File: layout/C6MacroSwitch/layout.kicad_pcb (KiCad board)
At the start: 2 copper layers, 70 x 85 mm, 32 parts, among them J1 S2B-PH-K-S(LF)(SN), J2 61300211121, SW1 CPG135001D01, SW2 CPG135001D01, SW3 CPG135001D01, SW4 CPG135001D01, SW5 CPG135001D01, SW6 CPG135001D01, SW7 TSA061B2808B, SW8 TSA061B2808B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

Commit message: feat(zener): resync layout KiCad ai LED 0603
Rigenerato il .kicad_pcb dopo il cambio package dei LED: i footprint
D_CHG/D_LED passano da LED_0402_1005Metric a LED_0603_1608Metric,
piazzamento preservato. Allinea il layout al design.
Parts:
- D1: value VLMS1500-GS08 -> LED RED; footprint kicad_libraries_kicad-footprints_LED_SMD@9.0.3:LED_0402_1005Metric -> kicad_libraries_kicad-footprints_LED_SMD@9.0.3:LED_0603_1608Metric
- D2: value VLMG1500-GS08 -> LED GREEN; footprint kicad_libraries_kicad-footprints_LED_SMD@9.0.3:LED_0402_1005Metric -> kicad_libraries_kicad-footprints_LED_SMD@9.0.3:LED_0603_1608Metric

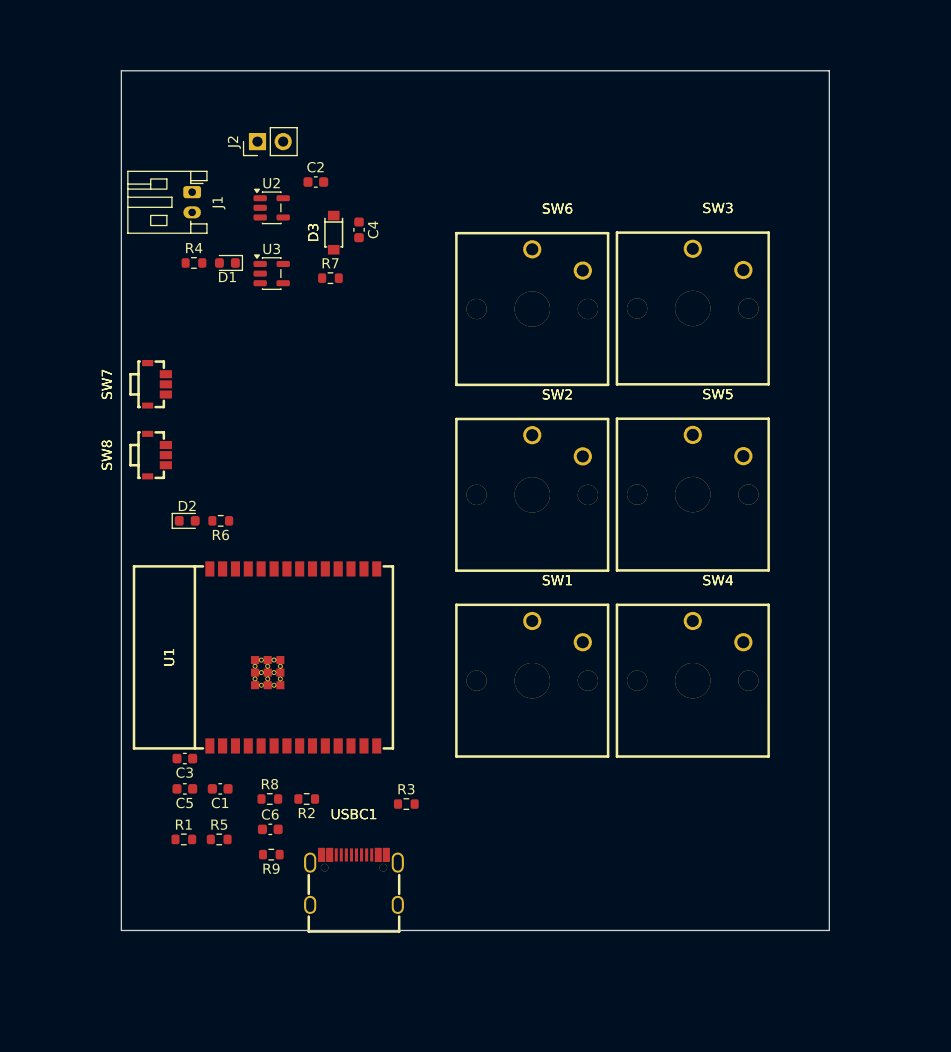
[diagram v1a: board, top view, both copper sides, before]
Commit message: feat(zener): piazza i 6 Choc su griglia 1u 2x3 (pitch 19.05mm)
Switch macro disposti su griglia 2x3 a pitch MX 1u (19.05mm) con stessa
rotazione; origine footprint compensata per l'offset del polo centrale
(-2.5,+4.85) così i centri keycap cadono su coordinate pulite. Nessuna
collisione Choc-Choc.

WIP floorplan: il cluster si sovrappone al supporto (ESP32/passivi),
da riposizionare sotto i tasti nella fase di layout finale.
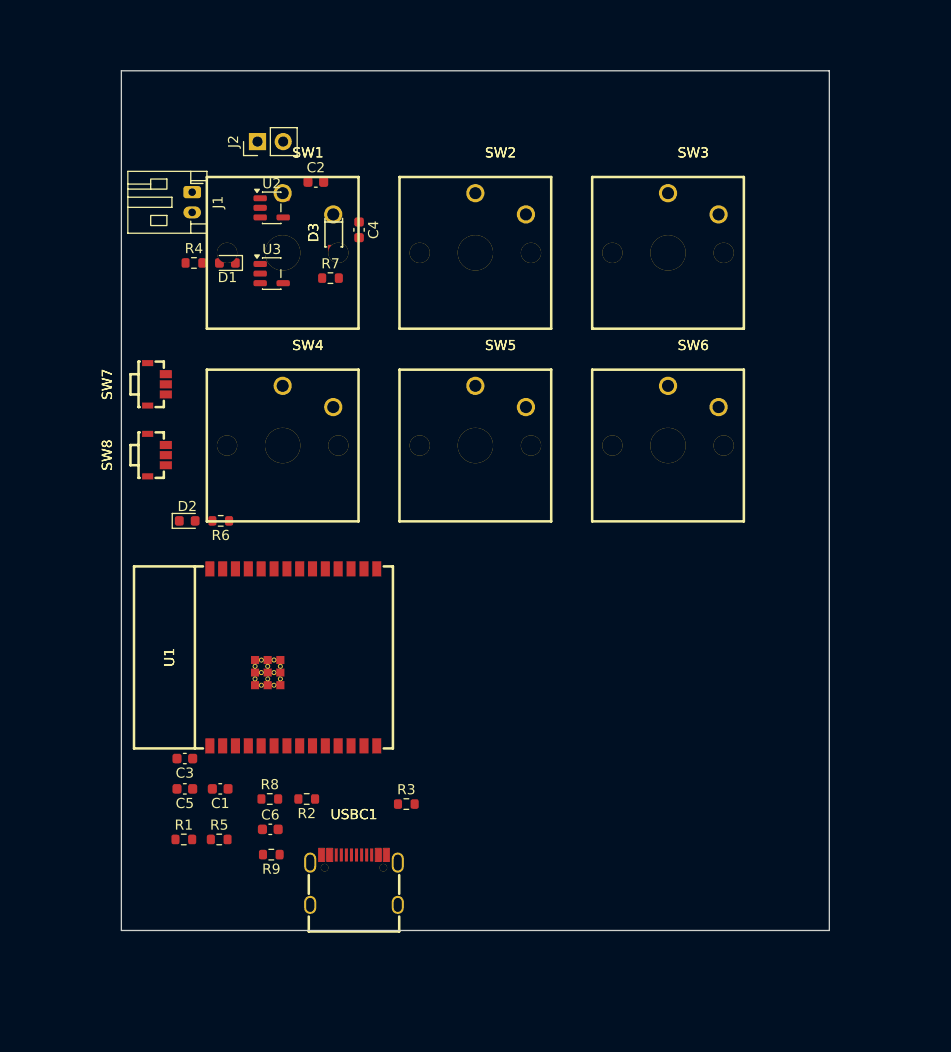
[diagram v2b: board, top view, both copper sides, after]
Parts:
- moved SW1 49.0 mm to (143.4, 63.1)
- moved SW4 46.7 mm to (143.4, 82.2)
- moved SW2 24.6 mm to (162.5, 63.1)
- moved SW5 22.0 mm to (162.5, 82.2)
- moved SW6 19.0 mm to (181.6, 82.2)
- moved SW3 6.02 mm to (181.6, 63.1)
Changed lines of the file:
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@@
 	(footprint "iu3qez_esp32c6_components_KailhChoc:KEY-TH_CPG135001D0X"
 		(layer "F.Cu")
-		(at 168.125 105.45)
+		(at 143.45 63.15)
 		(property "Reference" "SW1"
 			(at 0 -5.05 0)
@@
 	(footprint "iu3qez_esp32c6_components_KailhChoc:KEY-TH_CPG135001D0X"
 		(layer "F.Cu")
-		(at 184 68.65)
+		(at 181.55 63.15)
 		(property "Reference" "SW3"
 			(at 0 -5.05 0)
@@
 	(footprint "iu3qez_esp32c6_components_KailhChoc:KEY-TH_CPG135001D0X"
 		(layer "F.Cu")
-		(at 168.125 87.07675)
+		(at 162.5 63.15)
 		(property "Reference" "SW2"
 			(at 0 -5.05 0)
@@
 	(footprint "iu3qez_esp32c6_components_KailhChoc:KEY-TH_CPG135001D0X"
 		(layer "F.Cu")
-		(at 184 105.45)
+		(at 143.45 82.2)
 		(property "Reference" "SW4"
 			(at 0 -5.05 0)
@@
 	(footprint "iu3qez_esp32c6_components_KailhChoc:KEY-TH_CPG135001D0X"
 		(layer "F.Cu")
-		(at 184 87.05)
+		(at 162.5 82.2)
 		(property "Reference" "SW5"
 			(at 0 -5.05 0)
@@
 	(footprint "iu3qez_esp32c6_components_KailhChoc:KEY-TH_CPG135001D0X"
 		(layer "F.Cu")
-		(at 168.125 68.7035)
+		(at 181.55 82.2)
 		(property "Reference" "SW6"
 			(at 0 -5.05 0)

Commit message: feat(zener): primo sbroglio e layout della board
Prima passata di routing manuale in KiCad: 151 tracce, 17 via e 3 zone
di rame, con relative net class e impostazioni di progetto.
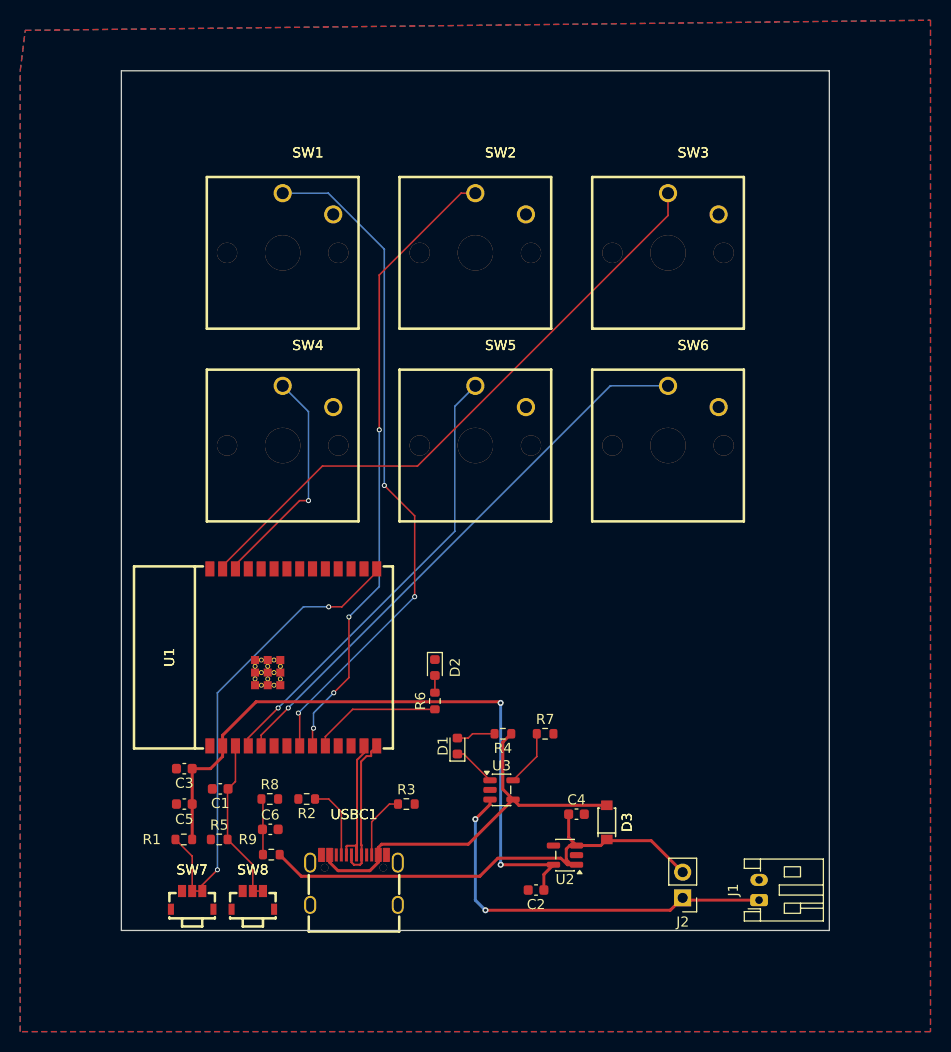
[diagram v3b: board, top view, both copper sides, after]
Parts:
- moved J1 89.7 mm to (188.1, 132.0), turned to 90 degrees
- moved J2 85.8 mm to (180.5, 131.8), turned to 180 degrees
- moved C2 73.3 mm to (166.0, 131.0), turned to 180 degrees
- moved U2 70.3 mm to (168.9, 127.5), turned to 180 degrees
- moved D3 64.3 mm to (173.0, 124.3), turned to 90 degrees
- moved C4 61.6 mm to (170.0, 123.5), turned to 0 degrees
- moved U3 55.9 mm to (162.6, 121.1)
- moved R4 55.7 mm to (162.7, 115.5), turned to 180 degrees
- moved D1 52.9 mm to (158.2, 116.8), turned to 90 degrees
- moved SW7 51.1 mm to (132.0, 132.0), turned to 180 degrees
- moved R7 49.8 mm to (166.9, 115.5)
- moved SW8 45.0 mm to (138.0, 132.0), turned to 180 degrees
- moved D2 28.5 mm to (156.0, 109.0), turned to -90 degrees
- moved R6 27.7 mm to (156.0, 112.3), turned to 90 degrees
- moved C5 1.50 mm to (131.2, 122.5)
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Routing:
- net KEY1: track 0.00 -> 67.5 mm, vias 0 -> 3
- net 3V3: track 0.00 -> 65.9 mm, vias 0 -> 2
- net KEY2: track 0.00 -> 62.1 mm, vias 0 -> 4
- net KEY3: track 0.00 -> 60.9 mm
- net KEY6: track 0.00 -> 55.6 mm, vias 0 -> 1
- net VBAT_SW: track 0.00 -> 50.1 mm
- net BOOT: track 0.00 -> 48.1 mm, vias 0 -> 2
- net KEY5: track 0.00 -> 44.9 mm, vias 0 -> 1
- net VBUS: track 0.00 -> 39.8 mm
- net VBAT: track 0.00 -> 39.6 mm, vias 0 -> 2
- net KEY4: track 0.00 -> 22.7 mm, vias 0 -> 1
- net EN: track 0.00 -> 16.7 mm
- net USB_D_P: track 0.00 -> 14.4 mm
- net USB_D_N: track 0.00 -> 13.8 mm
- net LED: track 0.00 -> 12.9 mm
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- added copper zone on B.Cu, net GND
- added copper zone on F.Cu, net GND

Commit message: fix(zener): review fixes — LDO caps 10uF, reverse-battery Q/D options, IO8 strap pullup, LED to IO10, Choc NPTH+courtyard
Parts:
- added D3: 1N5817W, iu3qez_esp32c6_components_SS1N5817W:SOD-123_L2.7-W1.6-LS3.6-RD, F.Cu at (197.2, 134.3)
- added Q1: AO3401A, iu3qez_esp32c6_components_AO3401A:SOT-23, F.Cu at (197.0, 127.7)
- added R6: ERJ-3EKF1002V, kicad_libraries_kicad-footprints_Resistor_SMD@9.0.3:R_0603_1608Metric, F.Cu at (200.9, 134.5)
- C4, C5: value GCM188R71E105KA64D -> GRM188Z71A106KA73D
- renumbered D3 to D4, R9 to R10, R6 to R7, R7 to R8, R8 to R9
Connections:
- J1 pad 1: VBAT -> BAT_RAW
- U1 pad 10: LED -> IO8_STRAP
- U1 pad 11: U1.IO10 -> LED

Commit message: fix(zener): LDO caps to 0805 for DC-bias derating margin
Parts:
- C4, C5: value GRM188Z71A106KA73D -> GRM21BZ71E106KE15K; footprint kicad_libraries_kicad-footprints_Capacitor_SMD@9.0.3:C_0603_1608Metric -> kicad_libraries_kicad-footprints_Capacitor_SMD@9.0.3:C_0805_2012Metric

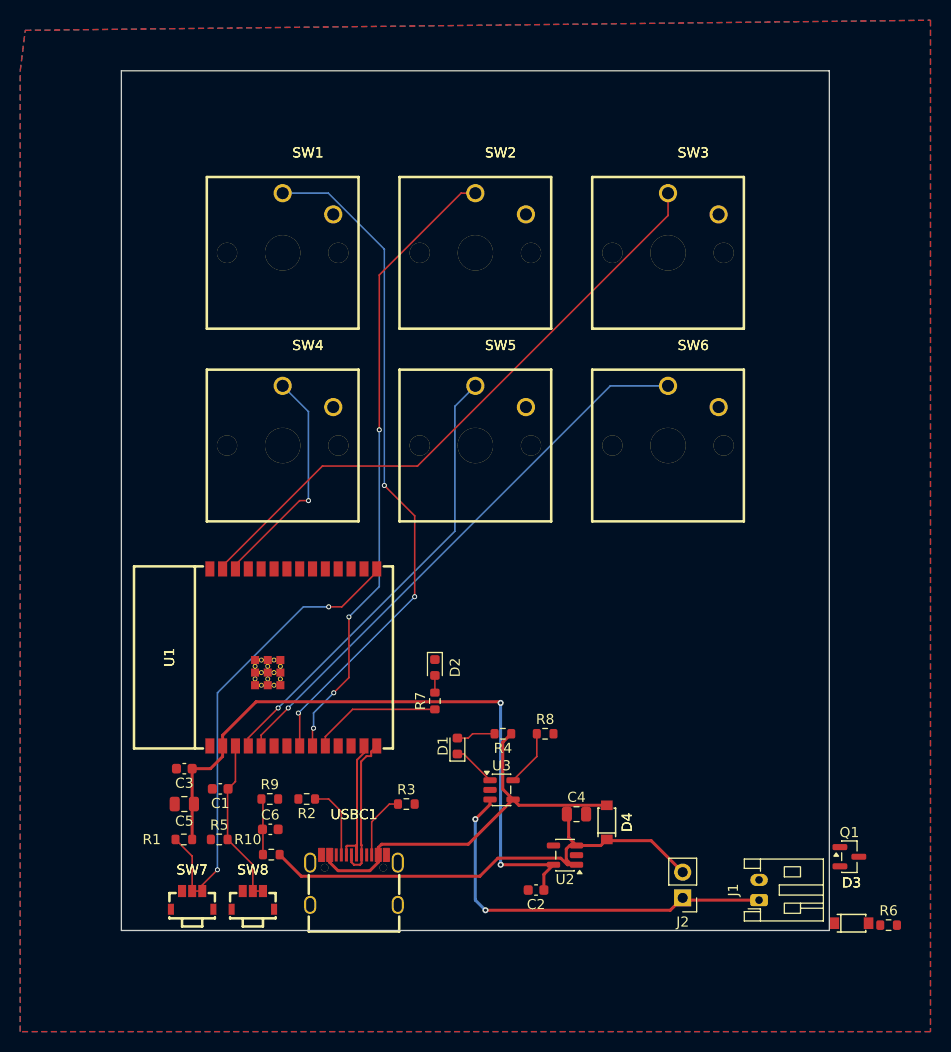
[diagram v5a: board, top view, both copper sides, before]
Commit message: feat(zener): 4x M3 corner mounting holes (GND) + 3mm rounded board corners
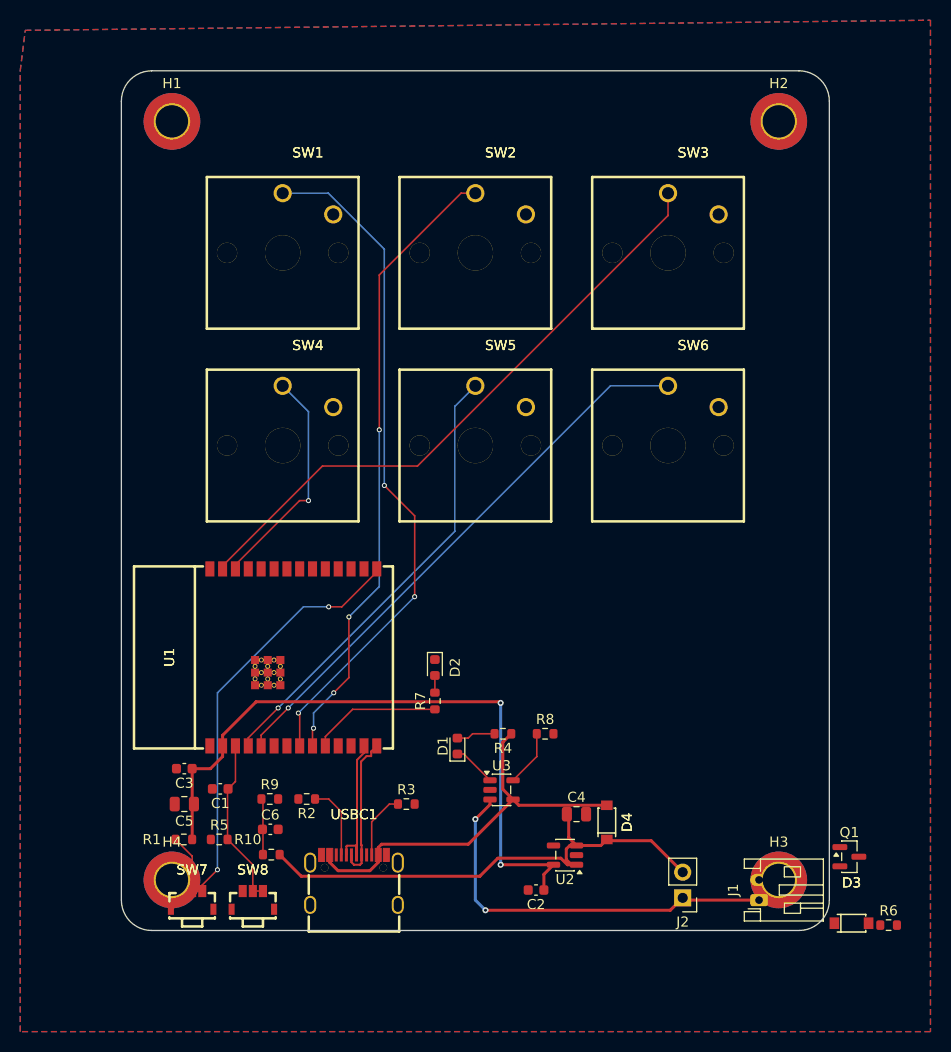
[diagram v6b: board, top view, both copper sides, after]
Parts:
- added H1: M3 DIN965 TopBottom, kicad_libraries_kicad-footprints_MountingHole@9.0.3:MountingHole_3.2mm_M3_DIN965_Pad_TopBottom, F.Cu at (130.0, 55.0)
- added H2: M3 DIN965 TopBottom, kicad_libraries_kicad-footprints_MountingHole@9.0.3:MountingHole_3.2mm_M3_DIN965_Pad_TopBottom, F.Cu at (190.0, 55.0)
- added H3: M3 DIN965 TopBottom, kicad_libraries_kicad-footprints_MountingHole@9.0.3:MountingHole_3.2mm_M3_DIN965_Pad_TopBottom, F.Cu at (190.0, 130.0)
- added H4: M3 DIN965 TopBottom, kicad_libraries_kicad-footprints_MountingHole@9.0.3:MountingHole_3.2mm_M3_DIN965_Pad_TopBottom, F.Cu at (130.0, 130.0)
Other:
- outline, holes or cut-outs redrawn

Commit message: feat(zener): ulteriore sbroglio e layout della board
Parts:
- moved R6 58.4 mm to (144.3, 119.9)
- moved D3 24.0 mm to (176.7, 121.8), turned to -90 degrees
- moved Q1 17.5 mm to (180.4, 122.0), turned to -90 degrees
- moved J2 16.5 mm to (176.5, 115.8), turned to -90 degrees
- moved J1 11.1 mm to (177.6, 128.2), turned to 0 degrees
- moved R4 8.87 mm to (158.6, 123.4)
- moved D1 4.00 mm to (156.8, 120.5), turned to -90 degrees
- moved SW7 3.34 mm to (135.3, 132.0)
- moved SW8 2.24 mm to (140.2, 132.0)
- moved R1 1.05 mm to (131.2, 125.0)
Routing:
- net VBAT: track 39.6 -> 26.2 mm, vias 2 -> 0
- net 3V3: track 65.9 -> 76.8 mm, vias 2 -> 4
- net BAT_RAW: track 0.00 -> 9.05 mm
- net VBAT_SENSE: track 5.56 -> 11.5 mm, vias 0 -> 2
- net VBUS: track 39.8 -> 35.5 mm
- net GND: track 0.00 -> 3.97 mm, vias 0 -> 8
- net IO8_STRAP: track 0.00 -> 3.16 mm
- net BOOT: track 48.1 -> 50.1 mm
- net VBAT_SW: track 50.1 -> 51.9 mm
- net LED: track 12.9 -> 11.2 mm
- net CHG_LED_A: track 3.85 -> 2.52 mm
- net EN: track 16.7 -> 17.6 mm
- net CHG_STAT: track 4.30 -> 4.83 mm
